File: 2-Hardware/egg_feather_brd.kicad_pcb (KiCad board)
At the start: 2 copper layers, 5 parts, among them SW1 SWITCH_SPST, U1 ADAFRUIT_FEATHER, U2 LIS3DH_BOB

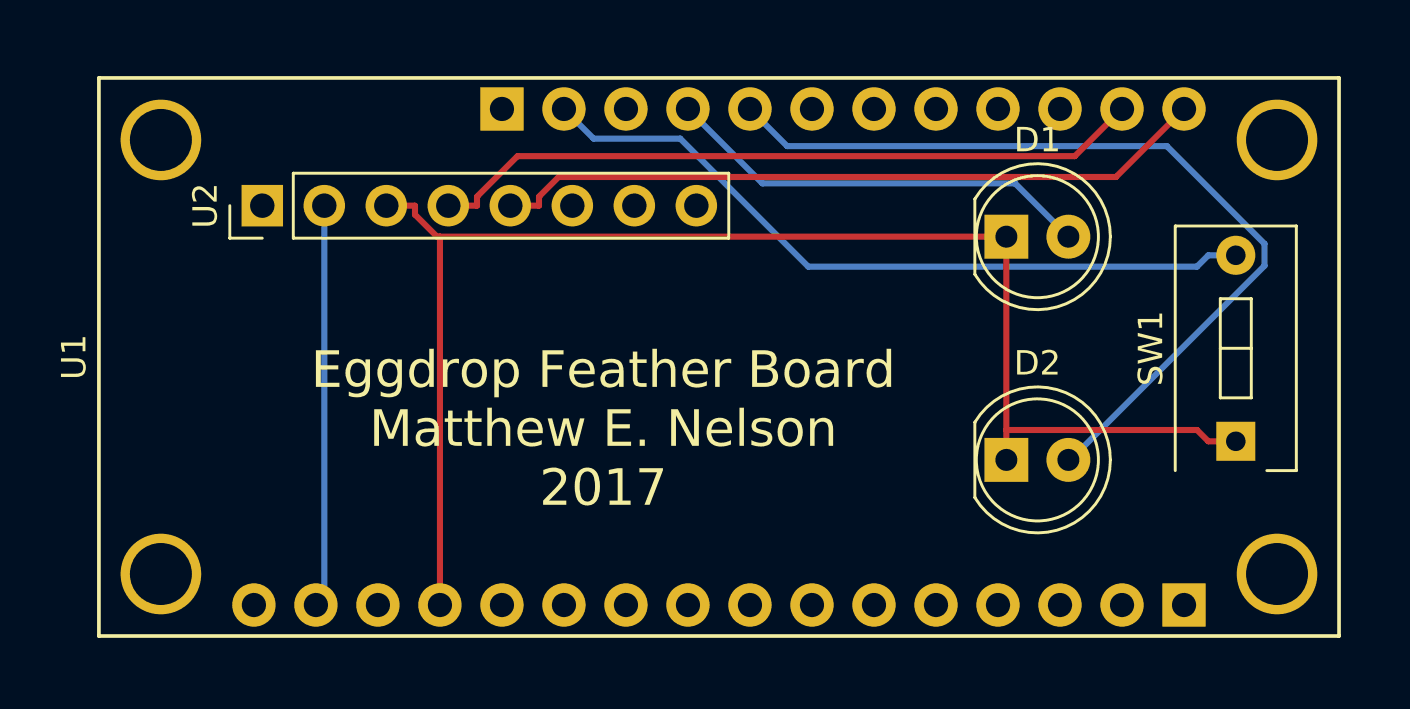
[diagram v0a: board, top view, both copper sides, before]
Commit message: Moved part off pin 13 to pin 11
Moved part off pin 13, new part placement on board
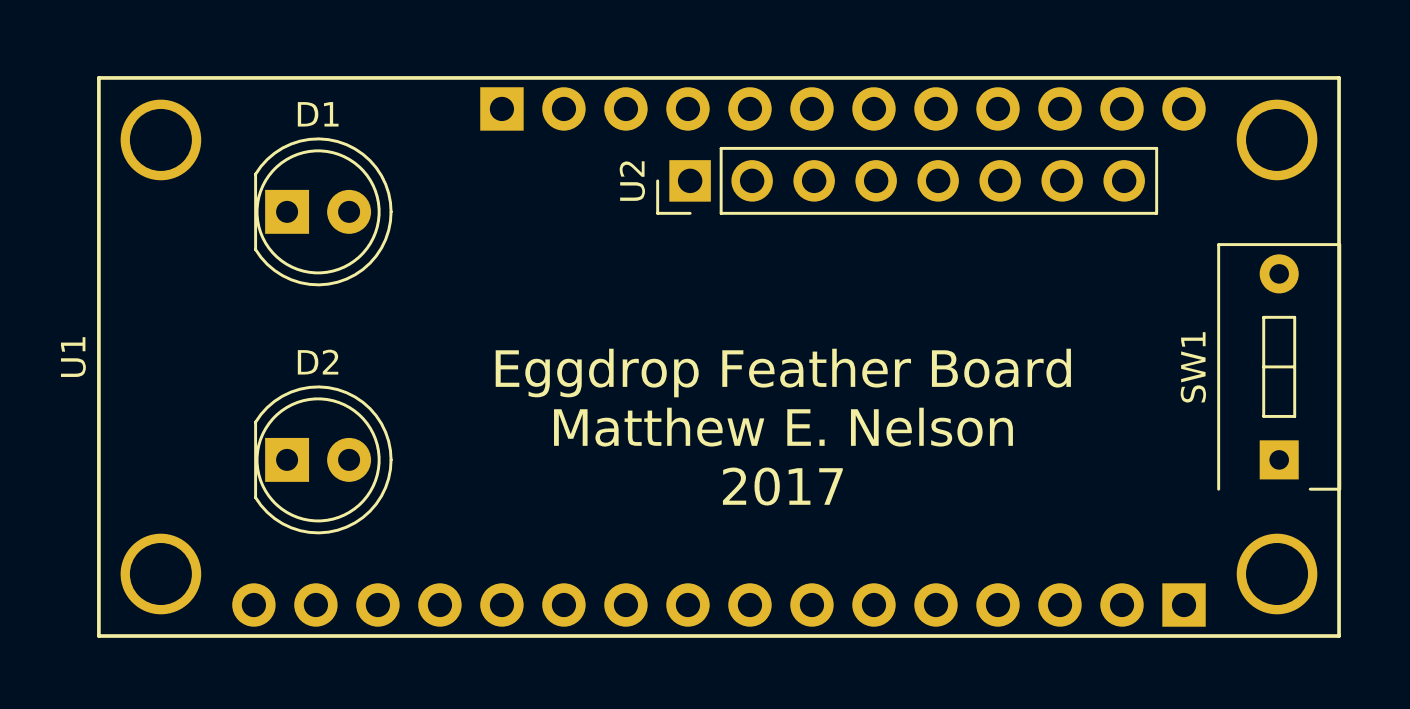
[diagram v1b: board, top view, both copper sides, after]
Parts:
- moved D1 29.5 mm to (130.8, 99.1)
- moved D2 29.5 mm to (130.8, 109.2)
- moved U2 17.6 mm to (147.3, 97.8)
- moved SW1 1.93 mm to (171.4, 109.2)
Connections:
- U1 pad 20: Net-(D1-Pad2) -> (no net)
- U1 pad 22: (no net) -> Net-(D1-Pad2)
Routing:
- net Net-(D1-Pad1): track 60.0 -> 0.00 mm
- net Net-(D2-Pad2): track 35.6 -> 0.00 mm
- net Net-(SW1-Pad2): track 30.4 -> 0.00 mm
- net Net-(U1-Pad28): track 29.5 -> 0.00 mm
- net Net-(U1-Pad27): track 29.5 -> 0.00 mm
- net Net-(D1-Pad2): track 17.8 -> 0.00 mm
- net Net-(U1-Pad15): track 16.5 -> 0.00 mm
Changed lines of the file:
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@@
   (general
     (links 10)
-    (no_connects 0)
-    (area 121.0601 93.298599 174.227 116.708601)
+    (no_connects 10)
+    (area 121.06 93.298999 176.005 116.709001)
     (thickness 1.6)
     (drawings 1)
-    (tracks 39)
+    (tracks 0)
     (zones 0)
     (modules 5)
@@
   )
   (module LEDs:LED_D5.0mm (layer F.Cu)
-    (at 160.274 100.076)
+    (at 130.81 99.06)
     (descr "LED, diameter 5.0mm, 2 pins, http://cdn-reichelt.de/documents/datenblatt/A500/LL-504BC2E-009.pdf")
     (tags "LED diameter 5.0mm 2 pins")
@@
   )
   (module LEDs:LED_D5.0mm (layer F.Cu)
-    (at 160.274 109.22)
+    (at 130.81 109.22)
     (descr "LED, diameter 5.0mm, 2 pins, http://cdn-reichelt.de/documents/datenblatt/A500/LL-504BC2E-009.pdf")
     (tags "LED diameter 5.0mm 2 pins")
@@
   )
   (module Buttons_Switches_THT:SW_DIP_x1_W7.62mm_Slide (layer F.Cu)
-    (at 169.672 108.458 90)
+    (at 171.45 109.22 90)
     (descr "1x-dip-switch, Slide, row spacing 7.62 mm (300 mils)")
     (tags "DIP Switch Slide 7.62mm 300mil")
@@
     (pad 17 thru_hole rect (at -8.89 -10.16) (size 1.778 1.778) (drill 0.9906) (layers *.Cu *.Mask F.SilkS))
     (pad 19 thru_hole circle (at -3.81 -10.16) (size 1.778 1.778) (drill 0.9906) (layers *.Cu *.Mask F.SilkS))
-    (pad 20 thru_hole circle (at -1.27 -10.16) (size 1.778 1.778) (drill 0.9906) (layers *.Cu *.Mask F.SilkS)
-      (net 2 "Net-(D1-Pad2)"))
+    (pad 20 thru_hole circle (at -1.27 -10.16) (size 1.778 1.778) (drill 0.9906) (layers *.Cu *.Mask F.SilkS))
     (pad 21 thru_hole circle (at 1.27 -10.16) (size 1.778 1.778) (drill 0.9906) (layers *.Cu *.Mask F.SilkS)
       (net 3 "Net-(D2-Pad2)"))
-    (pad 22 thru_hole circle (at 3.81 -10.16) (size 1.778 1.778) (drill 0.9906) (layers *.Cu *.Mask F.SilkS))
+    (pad 22 thru_hole circle (at 3.81 -10.16) (size 1.778 1.778) (drill 0.9906) (layers *.Cu *.Mask F.SilkS)
+      (net 2 "Net-(D1-Pad2)"))
     (pad 23 thru_hole circle (at 6.35 -10.16) (size 1.778 1.778) (drill 0.9906) (layers *.Cu *.Mask F.SilkS))
     (pad 24 thru_hole circle (at 8.89 -10.16) (size 1.778 1.778) (drill 0.9906) (layers *.Cu *.Mask F.SilkS))
@@
   )
   (module Pin_Headers:Pin_Header_Straight_1x08_Pitch2.54mm (layer F.Cu)
-    (at 129.794 98.806 90)
+    (at 147.32 97.79 90)
     (descr "Through hole straight pin header, 1x08, 2.54mm pitch, single row")
     (tags "Through hole pin header THT 1x08 2.54mm single row")
@@
     )
   )
-  (gr_text "Eggdrop Feather Board\nMatthew E. Nelson\n2017" (at 143.764 107.95) (layer F.SilkS)
+  (gr_text "Eggdrop Feather Board\nMatthew E. Nelson\n2017" (at 151.13 107.95) (layer F.SilkS)
     (effects (font (size 1.5 1.5) (thickness 0.3)))
   )
-  (segment (start 134.874 98.806) (end 136.0493 98.806) (width 0.25) (layer F.Cu) (net 1))
-  (segment (start 137.071 100.076) (end 137.071 115.164) (width 0.25) (layer F.Cu) (net 1))
-  (segment (start 136.952 100.076) (end 137.071 100.076) (width 0.25) (layer F.Cu) (net 1))
-  (segment (start 136.0493 99.1733) (end 136.952 100.076) (width 0.25) (layer F.Cu) (net 1))
-  (segment (start 136.0493 98.806) (end 136.0493 99.1733) (width 0.25) (layer F.Cu) (net 1))
-  (segment (start 137.071 100.076) (end 160.274 100.076) (width 0.25) (layer F.Cu) (net 1))
-  (segment (start 160.274 109.22) (end 160.274 107.9947) (width 0.25) (layer F.Cu) (net 1))
-  (segment (start 160.274 100.076) (end 160.274 107.9947) (width 0.25) (layer F.Cu) (net 1))
-  (segment (start 169.672 108.458) (end 168.5467 108.458) (width 0.25) (layer F.Cu) (net 1))
-  (segment (start 168.0834 107.9947) (end 160.274 107.9947) (width 0.25) (layer F.Cu) (net 1))
-  (segment (start 168.5467 108.458) (end 168.0834 107.9947) (width 0.25) (layer F.Cu) (net 1))
-  (segment (start 160.6324 97.8944) (end 162.814 100.076) (width 0.25) (layer B.Cu) (net 2))
-  (segment (start 150.2814 97.8944) (end 160.6324 97.8944) (width 0.25) (layer B.Cu) (net 2))
-  (segment (start 147.231 94.844) (end 150.2814 97.8944) (width 0.25) (layer B.Cu) (net 2))
-  (segment (start 162.814 109.2199) (end 162.814 109.22) (width 0.25) (layer B.Cu) (net 3))
-  (segment (start 162.8957 109.2199) (end 162.814 109.2199) (width 0.25) (layer B.Cu) (net 3))
-  (segment (start 170.8479 101.2677) (end 162.8957 109.2199) (width 0.25) (layer B.Cu) (net 3))
-  (segment (start 170.8479 100.3667) (end 170.8479 101.2677) (width 0.25) (layer B.Cu) (net 3))
-  (segment (start 166.8479 96.3667) (end 170.8479 100.3667) (width 0.25) (layer B.Cu) (net 3))
-  (segment (start 151.2937 96.3667) (end 166.8479 96.3667) (width 0.25) (layer B.Cu) (net 3))
-  (segment (start 149.771 94.844) (end 151.2937 96.3667) (width 0.25) (layer B.Cu) (net 3))
-  (segment (start 168.0806 101.3041) (end 168.5467 100.838) (width 0.25) (layer B.Cu) (net 4))
-  (segment (start 152.159 101.3041) (end 168.0806 101.3041) (width 0.25) (layer B.Cu) (net 4))
-  (segment (start 146.9133 96.0584) (end 152.159 101.3041) (width 0.25) (layer B.Cu) (net 4))
-  (segment (start 143.3654 96.0584) (end 146.9133 96.0584) (width 0.25) (layer B.Cu) (net 4))
-  (segment (start 142.151 94.844) (end 143.3654 96.0584) (width 0.25) (layer B.Cu) (net 4))
-  (segment (start 169.672 100.838) (end 168.5467 100.838) (width 0.25) (layer B.Cu) (net 4))
-  (segment (start 132.334 114.821) (end 131.991 115.164) (width 0.25) (layer B.Cu) (net 5))
-  (segment (start 132.334 98.806) (end 132.334 114.821) (width 0.25) (layer B.Cu) (net 5))
-  (segment (start 163.0764 96.7786) (end 165.011 94.844) (width 0.25) (layer F.Cu) (net 6))
-  (segment (start 140.2494 96.7786) (end 163.0764 96.7786) (width 0.25) (layer F.Cu) (net 6))
-  (segment (start 138.5893 98.4387) (end 140.2494 96.7786) (width 0.25) (layer F.Cu) (net 6))
-  (segment (start 138.5893 98.806) (end 138.5893 98.4387) (width 0.25) (layer F.Cu) (net 6))
-  (segment (start 137.414 98.806) (end 138.5893 98.806) (width 0.25) (layer F.Cu) (net 6))
-  (segment (start 164.7643 97.6307) (end 167.551 94.844) (width 0.25) (layer F.Cu) (net 7))
-  (segment (start 141.9372 97.6307) (end 164.7643 97.6307) (width 0.25) (layer F.Cu) (net 7))
-  (segment (start 141.1293 98.4386) (end 141.9372 97.6307) (width 0.25) (layer F.Cu) (net 7))
-  (segment (start 141.1293 98.806) (end 141.1293 98.4386) (width 0.25) (layer F.Cu) (net 7))
-  (segment (start 139.954 98.806) (end 141.1293 98.806) (width 0.25) (layer F.Cu) (net 7))
 )
